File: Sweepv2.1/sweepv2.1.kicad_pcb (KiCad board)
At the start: 2 copper layers, 217.4 x 86.9 mm, 51 parts, among them J1 AudioJack4dpb, J2 AudioJack4dpb, SW10 SW_Push, SW11 SW_Push, SW11_r1 SW_Push, SW12 SW_Push, SW12_r1 SW_Push, SW13_r1 SW_Push, SW14 SW_Push, SW15 SW_Push, SW15_r1 SW_Push, SW16 SW_Push, SW16_r1 SW_Push, SW17 SW_Push, SW17_r1 SW_Push, SW18 SW_Push, SW18_r1 SW_Push, SW2 SW_Push, SW20 SW_Push, SW20_r1 SW_Push, SW21 SW_Push, SW21_r1 SW_Push, SW2_r1 SW_Push, SW3 SW_Push, SW3_r1 SW_Push, SW4 SW_Push, SW4_r1 SW_Push, SW5 SW_Push, SW5_r1 SW_Push, SW6 SW_Push, SW6_r1 SW_Push, SW7_r1 SW_Push, SW8 SW_Push, SW8_r1 SW_Push, SW9 SW_Push, SW9_r1 SW_Push, U1 ProMicro-kbd, U2 ProMicro-kbd

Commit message: Refactor repository and fix breakaway tabs
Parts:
- removed the REF** at (75.7, 38.7)
- removed the REF** at (185.9, 38.7)
- removed the mouse-bite-2mm-slot at (130.6, 43.7)
- removed the mouse-bite-2mm-slot at (130.6, 67.6)
- added REF**: Tenting Puck, kbd:Tenting_Puck2, F.Cu at (75.7, 46.3)
- added REF**: Tenting Puck, kbd:Tenting_Puck2, F.Cu at (185.4, 46.3)
- added mouse-bite-2mm-slot: VAL**, Duckyb-Parts:mouse-bite-5mm-slot-with-space-for-track, F.Cu at (130.3, 51.3)
- added mouse-bite-2mm-slot: VAL**, Duckyb-Parts:mouse-bite-5mm-slot-with-space-for-track, F.Cu at (130.3, 75.2)
- moved J2 7.64 mm to (236.5, 86.1)
- moved RSW1 7.64 mm to (218.4, 83.1)
- moved SW14 7.64 mm to (139.9, 83.4)
- moved SW16 7.64 mm to (175.9, 64.5)
- moved SW8 7.64 mm to (139.9, 66.4)
- moved SW9 7.64 mm to (157.9, 54.4)
- moved SW_POWERR1 7.64 mm to (230.1, 51.8)
- moved SW18 7.64 mm to (211.8, 72.4)
- moved SW4 7.64 mm to (175.9, 30.4)
- moved SW10 7.64 mm to (175.9, 47.5)
- moved SW11 7.64 mm to (193.9, 52.8)
- moved SW15 7.64 mm to (157.9, 71.4)
- moved SW17 7.64 mm to (193.9, 69.8)
- moved SW2 7.64 mm to (139.9, 49.4)
- moved SW3 7.64 mm to (157.9, 37.4)
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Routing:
- net gnd: track 86.3 -> 40.7 mm
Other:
- board size 217.4 x 86.9 mm -> 216.9 x 86.9 mm

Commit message: Add gerbers
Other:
- outline, holes or cut-outs redrawn
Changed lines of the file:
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@@
   (gr_line (start 128.96 77.724) (end 128.975507 89.545022) (layer Edge.Cuts) (width 0.05))
   (gr_arc (start 22.542 50.442) (end 21.792 50.442) (angle 90) (layer Edge.Cuts) (width 0.05))
-  (gr_line (start 182.321777 21.502679) (end 178.120389 21.508139) (layer Edge.Cuts) (width 0.05))
+  (gr_line (start 182.067777 21.502679) (end 178.120389 21.508139) (layer Edge.Cuts) (width 0.05))
   (gr_arc (start 221.926148 81.404051) (end 236.953304 88.85815) (angle -25.93947102) (layer Edge.Cuts) (width 0.05))
   (gr_line (start 236.953304 88.85815) (end 226.446 107.451265) (layer Edge.Cuts) (width 0.05))
-  (gr_arc (start 177.866389 90.238139) (end 177.866389 21.508139) (angle -40.87028694) (layer Edge.Cuts) (width 0.05))
+  (gr_arc (start 177.866389 90.238139) (end 178.120389 21.508139) (angle -41.08203009) (layer Edge.Cuts) (width 0.05))
   (gr_line (start 222.033002 49.694917) (end 237.938 49.692) (layer Edge.Cuts) (width 0.05))
   (gr_line (start 219.998001 47.763999) (end 219.998045 30.439419) (layer Edge.Cuts) (width 0.05))

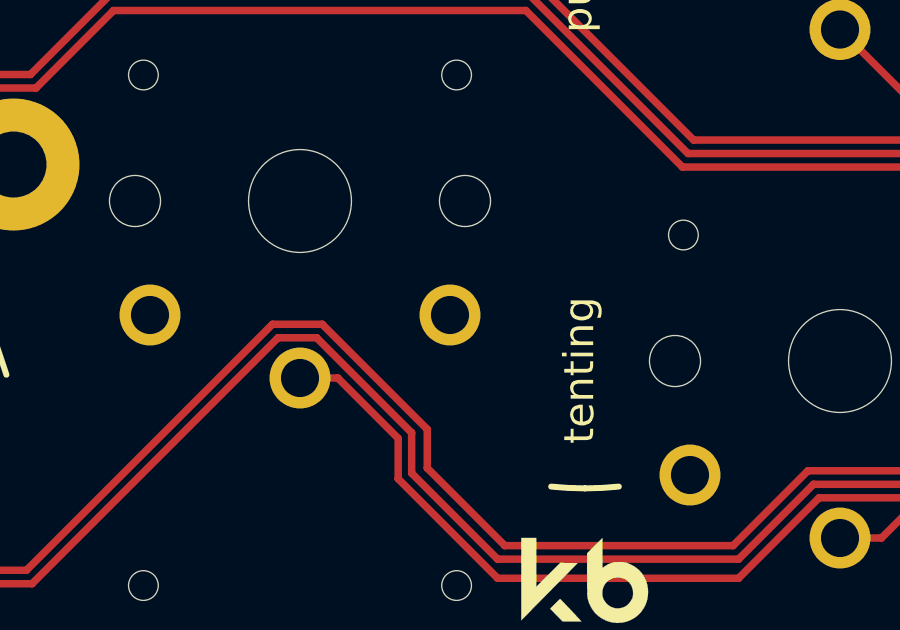
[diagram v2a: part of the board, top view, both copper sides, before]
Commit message: replace reversible switch footprint
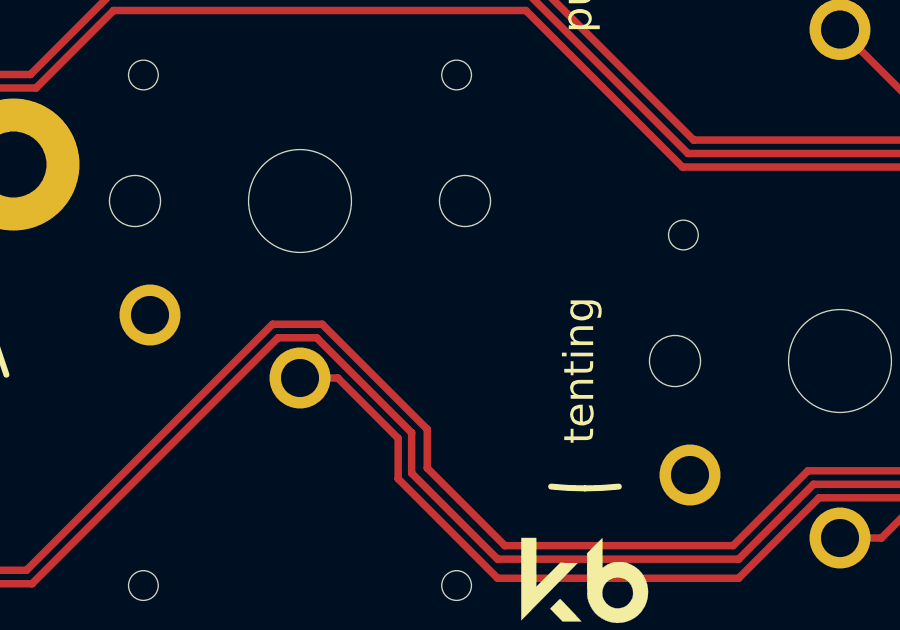
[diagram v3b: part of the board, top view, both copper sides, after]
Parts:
- SW10: footprint Kailh:SW_PG1350_rev_DPB -> Kailh:SW_PG1350_nonrev_DPB
